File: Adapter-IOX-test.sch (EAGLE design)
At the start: 51 parts, among them Q0 P-FET, Q1 P-FET, Q10 P-FET, Q11 P-FET, Q12 P-FET, Q13 P-FET, Q14 P-FET, Q15 P-FET, Q2 P-FET, Q3 P-FET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

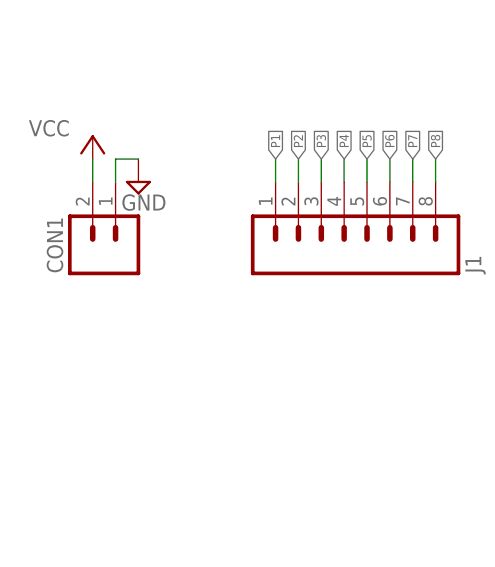
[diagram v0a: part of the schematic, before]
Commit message: higher density, narrow the board so 2x work with IOX-32
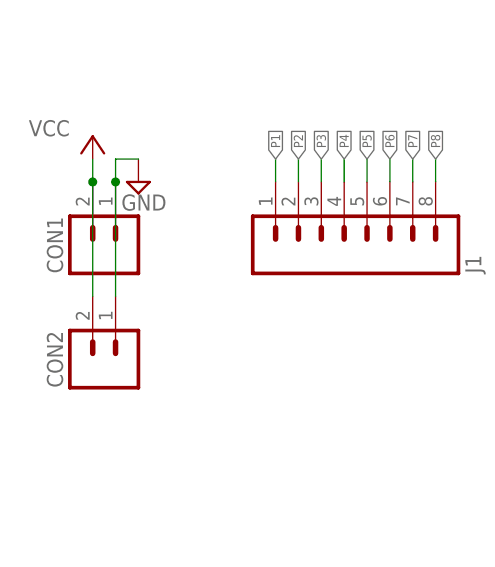
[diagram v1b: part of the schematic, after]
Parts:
- added CON2: (no value), SPCoast:CONNECTOR-M021X02-LOCK
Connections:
- net GND: now also CON2.A
- net VCC: now also CON2.B
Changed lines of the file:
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@@
 <part name="P+1" library="supply1" deviceset="VCC" device=""/>
 <part name="V1" library="supply2" deviceset="GND" device=""/>
+<part name="CON2" library="SPCoast" deviceset="CONNECTOR-M02" device="1X02-LOCK"/>
 </parts>
 <sheets>
@@
 </instance>
 <instance part="V1" gate="GND" x="20.32" y="60.96"/>
+<instance part="CON2" gate="J" x="17.78" y="43.18" rot="R90"/>
 </instances>
 <busses>
@@
 <pinref part="V1" gate="GND" pin="GND"/>
 <wire x1="17.78" y1="63.5" x2="20.32" y2="63.5" width="0.1524" layer="91"/>
+<pinref part="CON2" gate="J" pin="A"/>
+<wire x1="17.78" y1="60.96" x2="17.78" y2="48.26" width="0.1524" layer="91"/>
+<junction x="17.78" y="60.96"/>
 </segment>
 </net>
@@
 <wire x1="15.24" y1="60.96" x2="15.24" y2="63.5" width="0.1524" layer="91"/>
 <pinref part="P+1" gate="VCC" pin="VCC"/>
+<pinref part="CON2" gate="J" pin="B"/>
+<wire x1="15.24" y1="60.96" x2="15.24" y2="48.26" width="0.1524" layer="91"/>
+<junction x="15.24" y="60.96"/>
 </segment>
 </net>

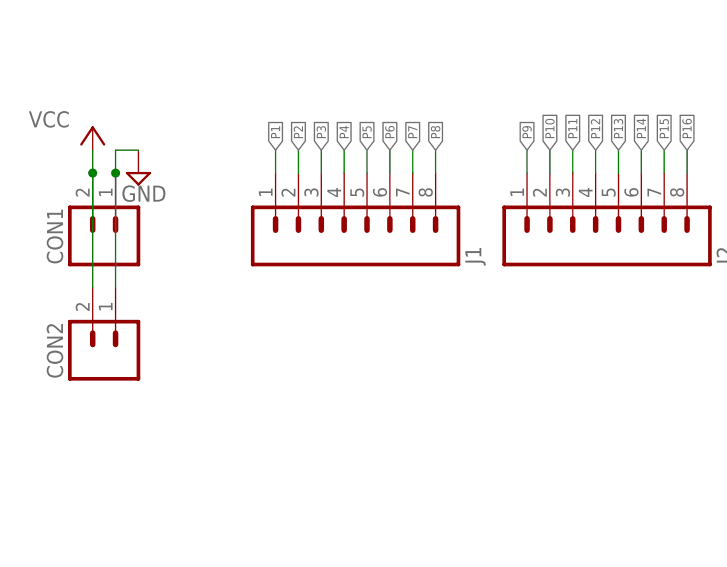
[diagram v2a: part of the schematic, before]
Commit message: added values for connectors
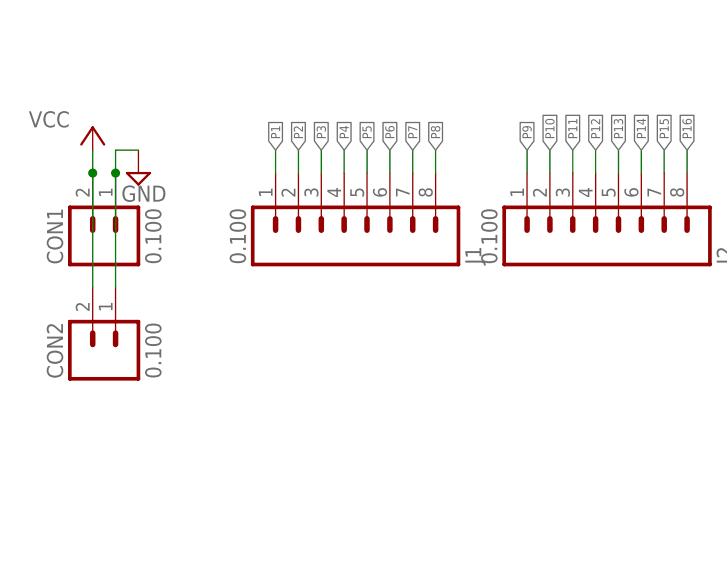
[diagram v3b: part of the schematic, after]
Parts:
- CON1, CON2, J1, J2: value (none) -> 0.100
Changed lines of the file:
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@@
 <part name="P+22" library="supply1" deviceset="VCC" device=""/>
 <part name="P+23" library="supply1" deviceset="VCC" device=""/>
-<part name="J1" library="SPCoast" deviceset="CONNECTOR-M08" device="LOCK"/>
-<part name="J2" library="SPCoast" deviceset="CONNECTOR-M08" device="LOCK"/>
-<part name="CON1" library="SPCoast" deviceset="CONNECTOR-M02" device="1X02-LOCK"/>
+<part name="J1" library="SPCoast" deviceset="CONNECTOR-M08" device="LOCK" value="0.100"/>
+<part name="J2" library="SPCoast" deviceset="CONNECTOR-M08" device="LOCK" value="0.100"/>
+<part name="CON1" library="SPCoast" deviceset="CONNECTOR-M02" device="1X02-LOCK" value="0.100"/>
 <part name="P+1" library="supply1" deviceset="VCC" device=""/>
 <part name="V1" library="supply2" deviceset="GND" device=""/>
-<part name="CON2" library="SPCoast" deviceset="CONNECTOR-M02" device="1X02-LOCK"/>
+<part name="CON2" library="SPCoast" deviceset="CONNECTOR-M02" device="1X02-LOCK" value="0.100"/>
 </parts>
 <sheets>
